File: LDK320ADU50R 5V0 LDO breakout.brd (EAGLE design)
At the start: 18 x 14 mm, 5 parts, among them IC1 LDK320ADU50R

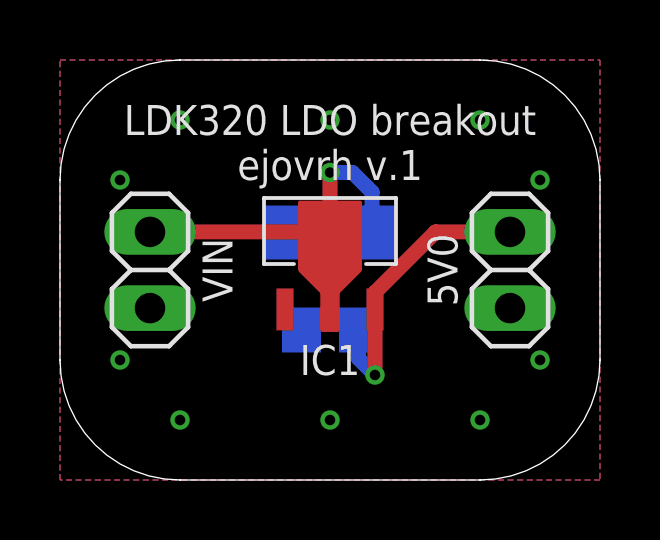
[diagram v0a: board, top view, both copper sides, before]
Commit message: - finished LDK320ADU50R 5V0 LDO breakout, created BOM, ran DRC & ERC
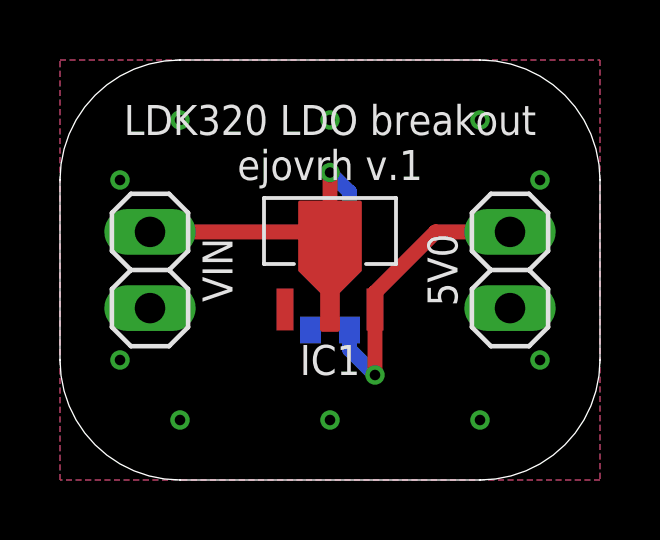
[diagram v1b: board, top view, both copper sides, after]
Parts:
- C1: device rcl:C0805 -> rcl:C0402
- C2: device rcl:C1206 -> rcl:C0402
- IC1: value LDK320ADU50R -> LDK320ADU50R
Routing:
- net VIN: track 13.6 -> 12.8 mm
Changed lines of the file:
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@@
 </autorouter>
 <elements>
-<element name="C1" library="rcl" library_urn="urn:adsk.eagle:library:334" package="C0805" package3d_urn="urn:adsk.eagle:package:23617/2" value="1μF" x="9" y="5" smashed="yes" rot="MR0">
+<element name="C1" library="rcl" library_urn="urn:adsk.eagle:library:334" package="C0402" package3d_urn="urn:adsk.eagle:package:23626/2" value="1μF" x="9" y="5" smashed="yes" rot="MR0">
 <attribute name="NAME" x="9" y="3.25" size="1" layer="26" font="vector" rot="MR0" align="center"/>
 <attribute name="SPICEPREFIX" value="C" x="-6.24" y="-8.97" size="1.778" layer="28" rot="MR0" display="off"/>
 <attribute name="VALUE" x="10.27" y="2.46" size="1.27" layer="28" rot="MR0"/>
 </element>
-<element name="C2" library="rcl" library_urn="urn:adsk.eagle:library:334" package="C1206" package3d_urn="urn:adsk.eagle:package:23618/2" value="1μF" x="9" y="8.25" smashed="yes" rot="MR180">
+<element name="C2" library="rcl" library_urn="urn:adsk.eagle:library:334" package="C0402" package3d_urn="urn:adsk.eagle:package:23626/2" value="1μF" x="9" y="8.25" smashed="yes" rot="MR180">
 <attribute name="NAME" x="9" y="10.25" size="1" layer="26" font="vector" rot="MR180" align="center"/>
 <attribute name="SPICEPREFIX" value="C" x="24.24" y="17.14" size="1.778" layer="28" rot="MR180" display="off"/>
 <attribute name="VALUE" x="7.73" y="10.79" size="1.27" layer="28" rot="MR180"/>
 </element>
-<element name="IC1" library="LDO SOT-89" package="SOT-89-D" value="  LDK320ADU50R" x="9" y="5" smashed="yes">
+<element name="IC1" library="LDO SOT-89" package="SOT-89-D" value="LDK320ADU50R" x="9" y="5" smashed="yes">
 <attribute name="NAME" x="9" y="4" size="1" layer="25" font="vector" align="center"/>
 <attribute name="VALUE" x="9" y="3.73" size="1" layer="27" font="vector" align="center"/>
@@
 <wire x1="9" y1="10.25" x2="9" y2="8.27" width="0.5" layer="1"/>
 <wire x1="9" y1="5.685" x2="9" y2="8.27" width="0.5" layer="1"/>
-<wire x1="10.4" y1="8.25" x2="10.4" y2="9.6" width="0.5" layer="16"/>
-<wire x1="10.4" y1="9.6" x2="9.75" y2="10.25" width="0.5" layer="16"/>
-<wire x1="9.75" y1="10.25" x2="9" y2="10.25" width="0.5" layer="16"/>
+<wire x1="9.65" y1="8.25" x2="9.65" y2="9.6" width="0.5" layer="16"/>
+<wire x1="9.65" y1="9.6" x2="9" y2="10.25" width="0.5" layer="16"/>
 </signal>
 <signal name="VOUT">
@@
 <wire x1="10.5" y1="5.685" x2="10.5" y2="3.5" width="0.5" layer="1"/>
 <via x="10.5" y="3.5" extent="1-16" drill="0.35"/>
-<wire x1="10.5" y1="3.5" x2="9.95" y2="4.05" width="0.5" layer="16"/>
-<wire x1="9.95" y1="4.05" x2="9.95" y2="5" width="0.5" layer="16"/>
 <wire x1="15" y1="8.27" x2="12.52" y2="8.27" width="0.5" layer="1"/>
 <wire x1="12.52" y1="8.27" x2="10.5" y2="6.25" width="0.5" layer="1"/>
 <wire x1="10.5" y1="6.25" x2="10.5" y2="5.685" width="0.5" layer="1"/>
+<wire x1="9.65" y1="5" x2="9.65" y2="4.35" width="0.5" layer="16"/>
+<wire x1="9.65" y1="4.35" x2="10.5" y2="3.5" width="0.5" layer="16"/>
 </signal>
 <signal name="GND">
